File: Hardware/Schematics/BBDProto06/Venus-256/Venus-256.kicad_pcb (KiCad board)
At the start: 4 copper layers, 180.1 x 113.7 mm, 231 parts, among them J201 RaspberryPi header, J301 ARM JTAG, U1001 AD7616, U101 TPS22993, U401 AD7616, U501 ATSAME70Q21A-AN, U601 AD7616, U701 AD7616, U801 AD7616, U901 ATSAME70Q21A-AN

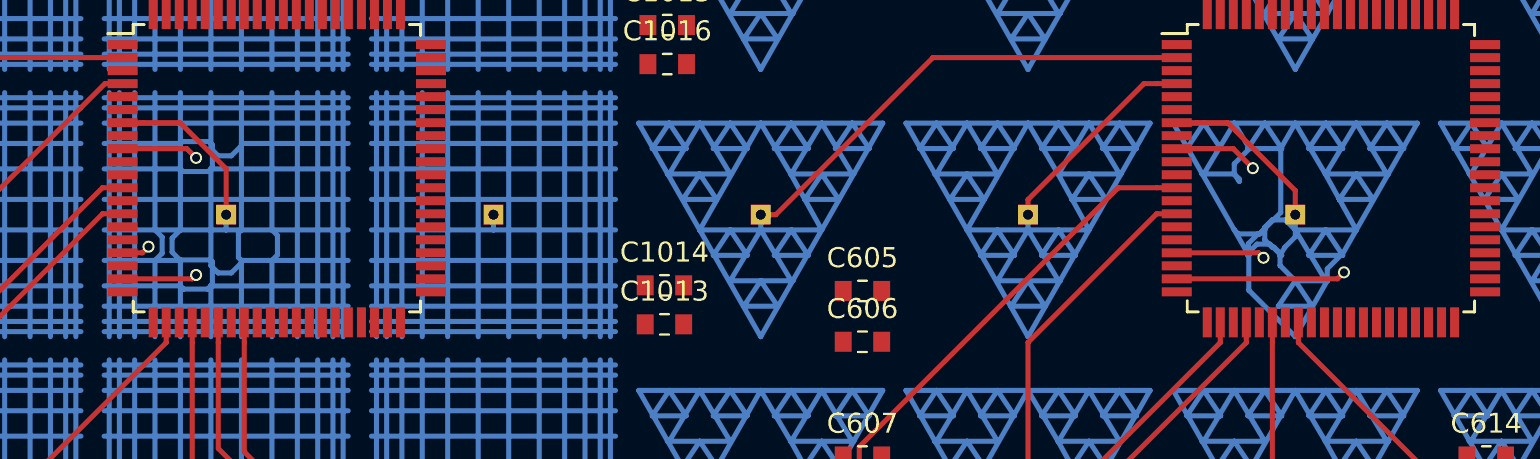
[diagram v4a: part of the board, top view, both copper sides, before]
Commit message: Fixed the antenna net mess-up
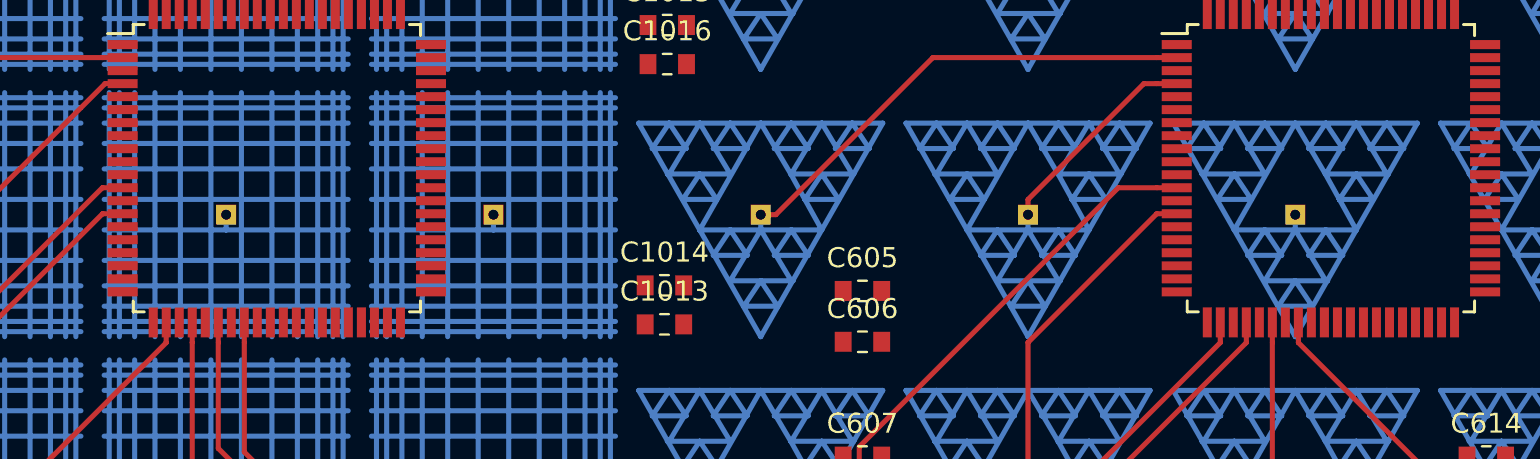
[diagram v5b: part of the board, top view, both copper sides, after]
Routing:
- net Net-(TP405-Pad1): track 219.9 -> 125.8 mm
- net Net-(TP602-Pad1): track 82.6 -> 129.6 mm
- net Net-(TP603-Pad1): track 91.7 -> 138.7 mm
- net Net-(TP609-Pad1): track 150.0 -> 125.8 mm, vias 1 -> 0
- net Net-(TP1009-Pad1): track 316.3 -> 293.4 mm, vias 1 -> 0
- net Net-(TP605-Pad1): track 146.5 -> 125.8 mm, vias 1 -> 0
- net Net-(TP1005-Pad1): track 313.3 -> 293.4 mm, vias 1 -> 0
- net Net-(TP610-Pad1): track 142.1 -> 125.8 mm, vias 1 -> 0
- net Net-(TP1010-Pad1): track 308.1 -> 293.4 mm, vias 1 -> 0
- net Net-(TP1006-Pad1): track 304.7 -> 293.4 mm
- net Net-(TP606-Pad1): track 129.5 -> 125.8 mm

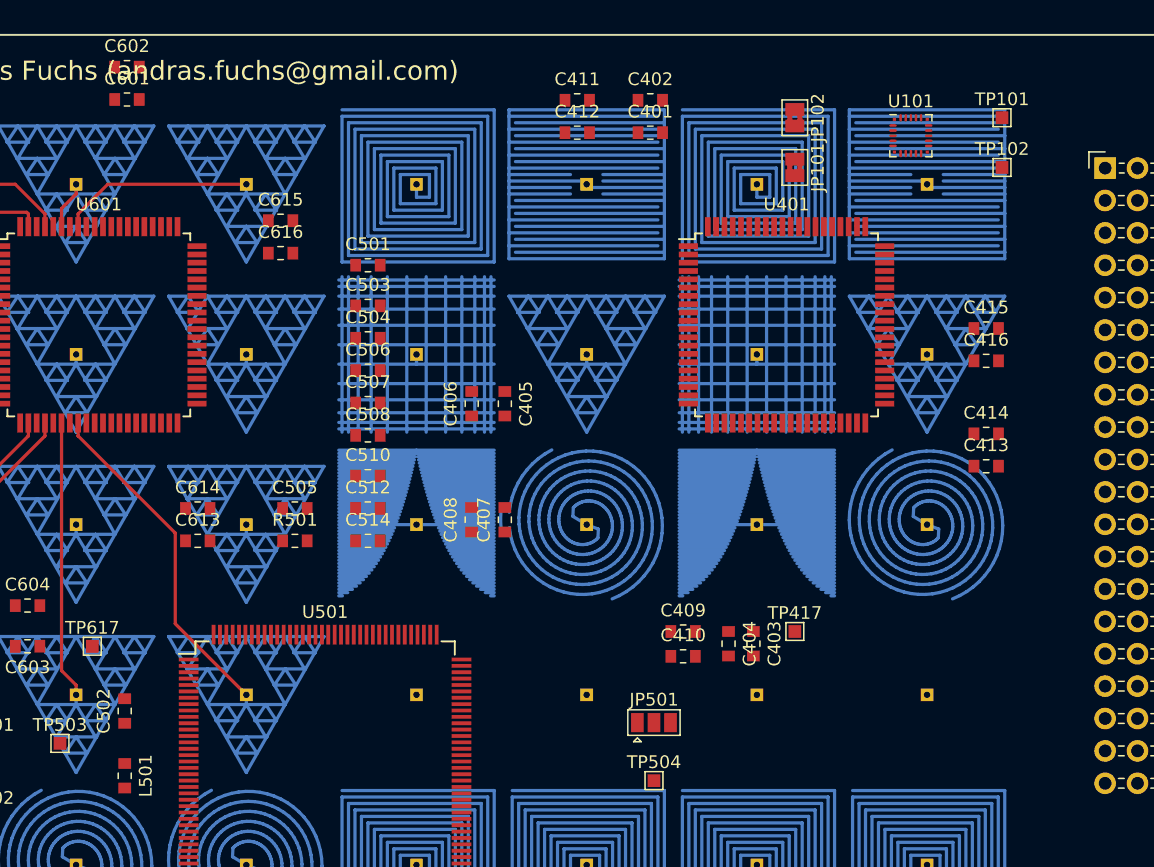
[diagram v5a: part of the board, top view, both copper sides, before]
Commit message: Removed a few tracks
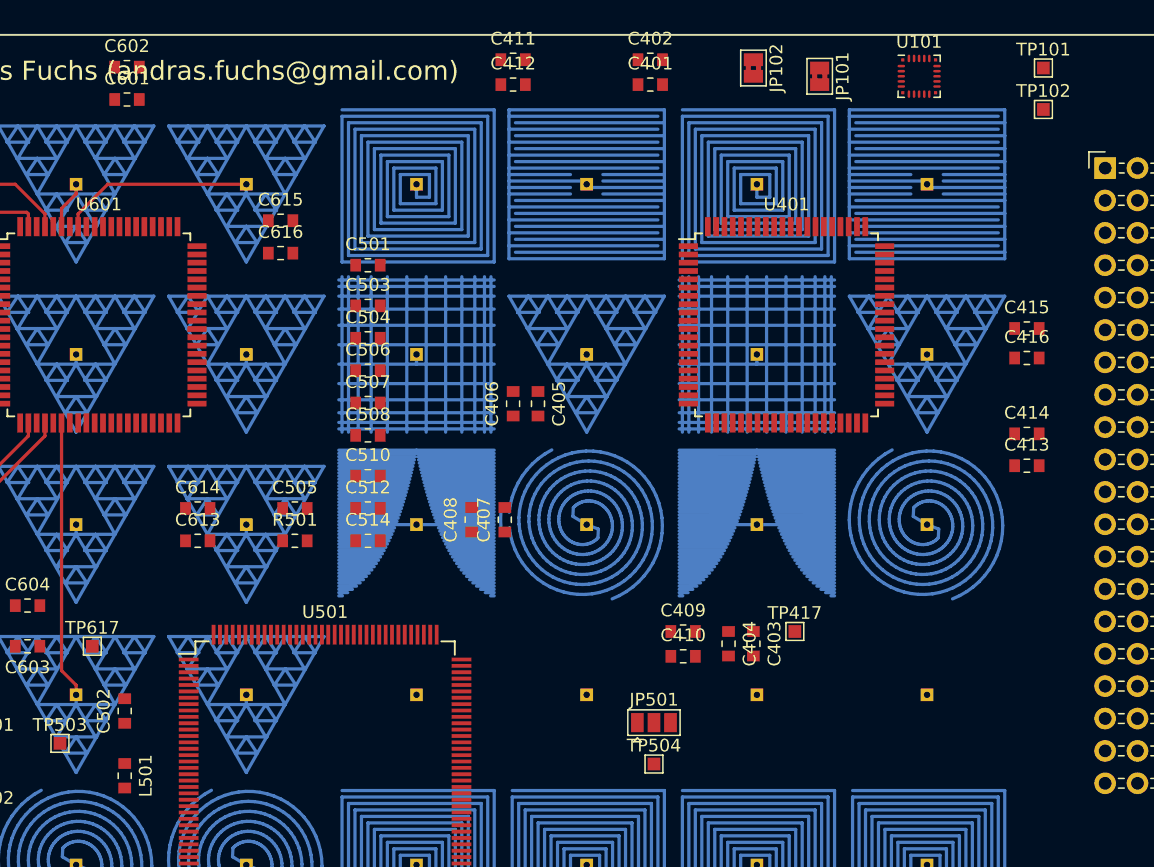
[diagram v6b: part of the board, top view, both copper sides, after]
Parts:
- moved JP101 7.41 mm to (165.1, 18.2)
- moved C412 6.29 mm to (141.1, 18.9)
- moved C411 5.95 mm to (141.1, 16.9)
- moved TP102 5.59 mm to (182.7, 20.8)
- moved JP102 5.08 mm to (159.9, 17.6)
- moved TP101 5.08 mm to (182.7, 17.6)
- moved U101 4.71 mm to (172.9, 18.2)
- moved C401 3.77 mm to (151.8, 18.9)
- moved C406 3.25 mm to (141.1, 43.9)
- moved C416 3.20 mm to (181.3, 40.3)
- moved C413 3.19 mm to (181.3, 48.8)
- moved C414 3.19 mm to (181.3, 46.2)
- moved C415 3.19 mm to (181.3, 38.0)
- moved C402 3.18 mm to (151.8, 16.9)
- moved C405 2.60 mm to (143.0, 43.9)
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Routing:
- net Net-(TP613-Pad1): track 152.6 -> 125.8 mm
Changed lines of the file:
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@@
     (thickness 1.6)
     (drawings 247)
-    (tracks 15846)
+    (tracks 15841)
     (zones 0)
     (modules 231)
@@
     (pad_to_mask_clearance 0.2)
     (aux_axis_origin 14.95 14.95)
-    (visible_elements 7FFFF7FF)
+    (visible_elements 7FFFFFFF)
     (pcbplotparams
       (layerselection 0x010fc_ffffffff)
@@
   )
   (module Capacitor_SMD:C_0603_1608Metric_Pad0.84x1.00mm_HandSolder (layer F.Cu)
-    (at 140.4 43.8875 270)
+    (at 143 43.8875 270)
     (descr "Capacitor SMD 0603 (1608 Metric), square (rectangular) end terminal, IPC_7351 nominal with elongated pad for handsoldering. (Body size source: http://www.tortai-tech.com/upload/download/2011102023233369053.pdf), generated with kicad-footprint-generator")
     (tags "capacitor handsolder")
@@
   )
   (module Capacitor_SMD:C_0603_1608Metric_Pad0.84x1.00mm_HandSolder (layer F.Cu)
-    (at 137.8 43.8875 90)
+    (at 141.05 43.8875 90)
     (descr "Capacitor SMD 0603 (1608 Metric), square (rectangular) end terminal, IPC_7351 nominal with elongated pad for handsoldering. (Body size source: http://www.tortai-tech.com/upload/download/2011102023233369053.pdf), generated with kicad-footprint-generator")
     (tags "capacitor handsolder")
@@
   )
   (module Capacitor_SMD:C_0603_1608Metric_Pad0.84x1.00mm_HandSolder (layer F.Cu)
-    (at 178.16 46.25)
+    (at 181.35 46.25)
     (descr "Capacitor SMD 0603 (1608 Metric), square (rectangular) end terminal, IPC_7351 nominal with elongated pad for handsoldering. (Body size source: http://www.tortai-tech.com/upload/download/2011102023233369053.pdf), generated with kicad-footprint-generator")
     (tags "capacitor handsolder")
@@
   )
   (module Capacitor_SMD:C_0603_1608Metric_Pad0.84x1.00mm_HandSolder (layer F.Cu)
-    (at 178.16 48.79)
+    (at 181.35 48.75)
     (descr "Capacitor SMD 0603 (1608 Metric), square (rectangular) end terminal, IPC_7351 nominal with elongated pad for handsoldering. (Body size source: http://www.tortai-tech.com/upload/download/2011102023233369053.pdf), generated with kicad-footprint-generator")
     (tags "capacitor handsolder")
@@
   )
   (module Capacitor_SMD:C_0603_1608Metric_Pad0.84x1.00mm_HandSolder (layer F.Cu)
-    (at 146.08 20.08)
+    (at 141.05 16.9)
     (descr "Capacitor SMD 0603 (1608 Metric), square (rectangular) end terminal, IPC_7351 nominal with elongated pad for handsoldering. (Body size source: http://www.tortai-tech.com/upload/download/2011102023233369053.pdf), generated with kicad-footprint-generator")
     (tags "capacitor handsolder")
@@
   )
   (module Capacitor_SMD:C_0603_1608Metric_Pad0.84x1.00mm_HandSolder (layer F.Cu)
-    (at 146.08 22.62)
+    (at 141.05 18.85)
     (descr "Capacitor SMD 0603 (1608 Metric), square (rectangular) end terminal, IPC_7351 nominal with elongated pad for handsoldering. (Body size source: http://www.tortai-tech.com/upload/download/2011102023233369053.pdf), generated with kicad-footprint-generator")
     (tags "capacitor handsolder")
@@
   )
   (module Capacitor_SMD:C_0603_1608Metric_Pad0.84x1.00mm_HandSolder (layer F.Cu)
-    (at 151.81 20.08)
+    (at 151.81 16.9)
     (descr "Capacitor SMD 0603 (1608 Metric), square (rectangular) end terminal, IPC_7351 nominal with elongated pad for handsoldering. (Body size source: http://www.tortai-tech.com/upload/download/2011102023233369053.pdf), generated with kicad-footprint-generator")
     (tags "capacitor handsolder")
@@
   )
   (module Capacitor_SMD:C_0603_1608Metric_Pad0.84x1.00mm_HandSolder (layer F.Cu)
-    (at 151.81 22.62)
+    (at 151.81 18.85)
     (descr "Capacitor SMD 0603 (1608 Metric), square (rectangular) end terminal, IPC_7351 nominal with elongated pad for handsoldering. (Body size source: http://www.tortai-tech.com/upload/download/2011102023233369053.pdf), generated with kicad-footprint-generator")
     (tags "capacitor handsolder")
@@
   )
   (module Capacitor_SMD:C_0603_1608Metric_Pad0.84x1.00mm_HandSolder (layer F.Cu)
-    (at 178.16 37.98)
+    (at 181.35 37.98)
     (descr "Capacitor SMD 0603 (1608 Metric), square (rectangular) end terminal, IPC_7351 nominal with elongated pad for handsoldering. (Body size source: http://www.tortai-tech.com/upload/download/2011102023233369053.pdf), generated with kicad-footprint-generator")
     (tags "capacitor handsolder")
@@
   )
   (module Capacitor_SMD:C_0603_1608Metric_Pad0.84x1.00mm_HandSolder (layer F.Cu)
-    (at 178.16 40.52)
+    (at 181.35 40.3)
     (descr "Capacitor SMD 0603 (1608 Metric), square (rectangular) end terminal, IPC_7351 nominal with elongated pad for handsoldering. (Body size source: http://www.tortai-tech.com/upload/download/2011102023233369053.pdf), generated with kicad-footprint-generator")
     (tags "capacitor handsolder")
@@
   )
   (module TestPoint:TestPoint_Pad_1.0x1.0mm (layer F.Cu)
-    (at 179.4 21.45)
+    (at 182.65 17.55)
     (descr "SMD rectangular pad as test Point, square 1.0mm side length")
     (tags "test point SMD pad rectangle square")
@@
   )
   (module TestPoint:TestPoint_Pad_1.0x1.0mm (layer F.Cu)
-    (at 179.4 25.35)
+    (at 182.65 20.8)
     (descr "SMD rectangular pad as test Point, square 1.0mm side length")
     (tags "test point SMD pad rectangle square")
@@
   )
   (module Package_DFN_QFN:Texas_S-PWQFN-N20 (layer F.Cu)
-    (at 172.25 22.86)
+    (at 172.9 18.2)
     (descr "20-Pin Plastic Quad Flatpack No-Lead Package, Body 3.0x3.0x0.8mm, Texas Instruments (http://www.ti.com/lit/ds/symlink/tps22993.pdf)")
     (tags "QFN 0.4")
@@
   )
   (module Jumper:SolderJumper-2_P1.3mm_Bridged2Bar_Pad1.0x1.5mm (layer F.Cu)
-    (at 163.15 25.35 270)
+    (at 165.1 18.2 270)
     (descr "SMD Solder Jumper, 1x1.5mm Pads, 0.3mm gap, bridged with 2 copper strips")
     (tags "solder jumper open")
@@
   )
   (module Jumper:SolderJumper-2_P1.3mm_Bridged2Bar_Pad1.0x1.5mm (layer F.Cu)
-    (at 163.15 21.45 270)
+    (at 159.9 17.55 270)
     (descr "SMD Solder Jumper, 1x1.5mm Pads, 0.3mm gap, bridged with 2 copper strips")
     (tags "solder jumper open")
@@
   )
   (module TestPoint:TestPoint_Pad_1.0x1.0mm (layer F.Cu)
-    (at 152.1 73.45)
+    (at 152.1 72.15)
     (descr "SMD rectangular pad as test Point, square 1.0mm side length")
     (tags "test point SMD pad rectangle square")
@@
   (segment (start 117.072 64.688) (end 115.548 64.688) (width 0.254) (layer B.Cu) (net 70))
   (segment (start 115.548 64.688) (end 115.4754 64.688) (width 0.254) (layer B.Cu) (net 70))
-  (segment (start 106.925 46.404) (end 106.925 45.4) (width 0.254) (layer F.Cu) (net 70))
-  (segment (start 106.925 46.410802) (end 106.925 46.404) (width 0.254) (layer F.Cu) (net 70))
-  (segment (start 114.543999 54.029801) (end 106.925 46.410802) (width 0.254) (layer F.Cu) (net 70))
-  (segment (start 114.543999 61.143999) (end 114.543999 54.029801) (width 0.254) (layer F.Cu) (net 70))
-  (segment (start 120.12 66.72) (end 114.543999 61.143999) (width 0.254) (layer F.Cu) (net 70))
   (segment (start 106.77 70.022) (end 105.923 71.292) (width 0.254) (layer B.Cu) (net 71))
   (segment (start 105.923 71.292) (end 107.617 71.292) (width 0.254) (layer B.Cu) (net 71))

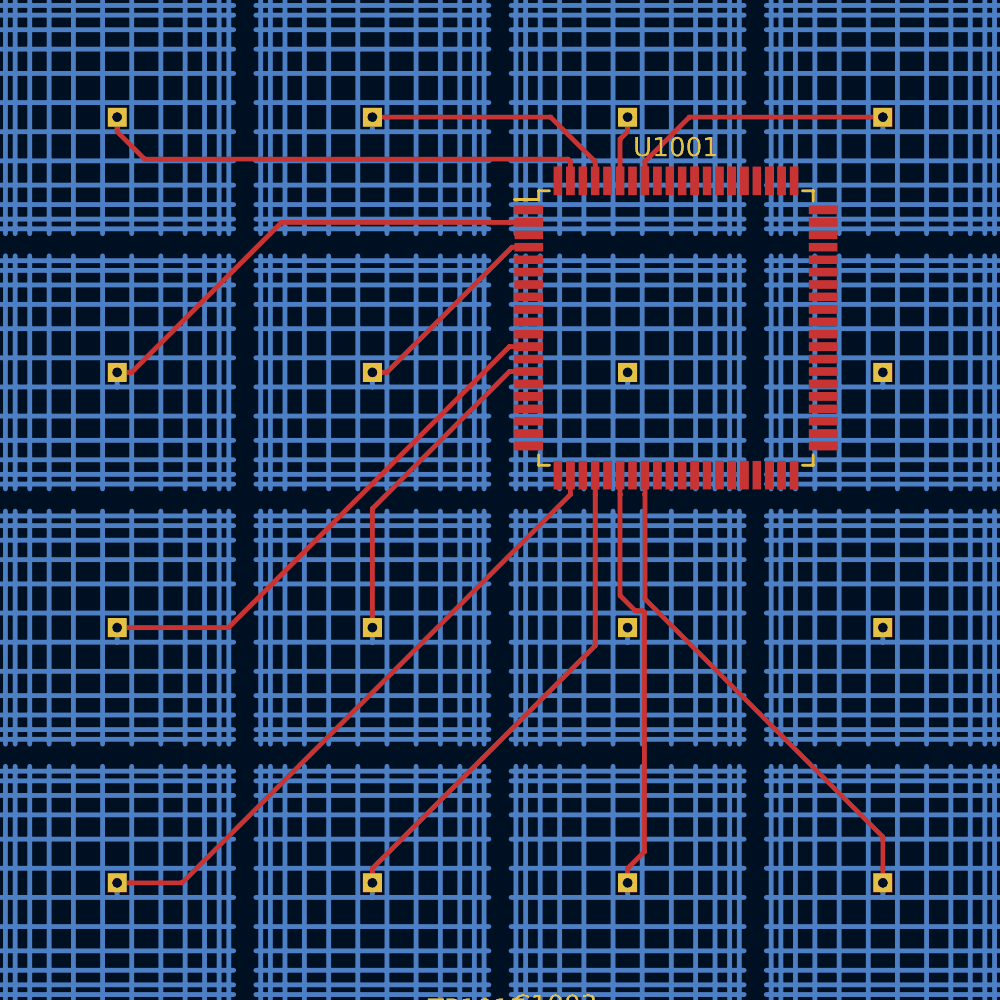
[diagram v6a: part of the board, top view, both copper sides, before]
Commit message: Connected the sensors to U1001 manually
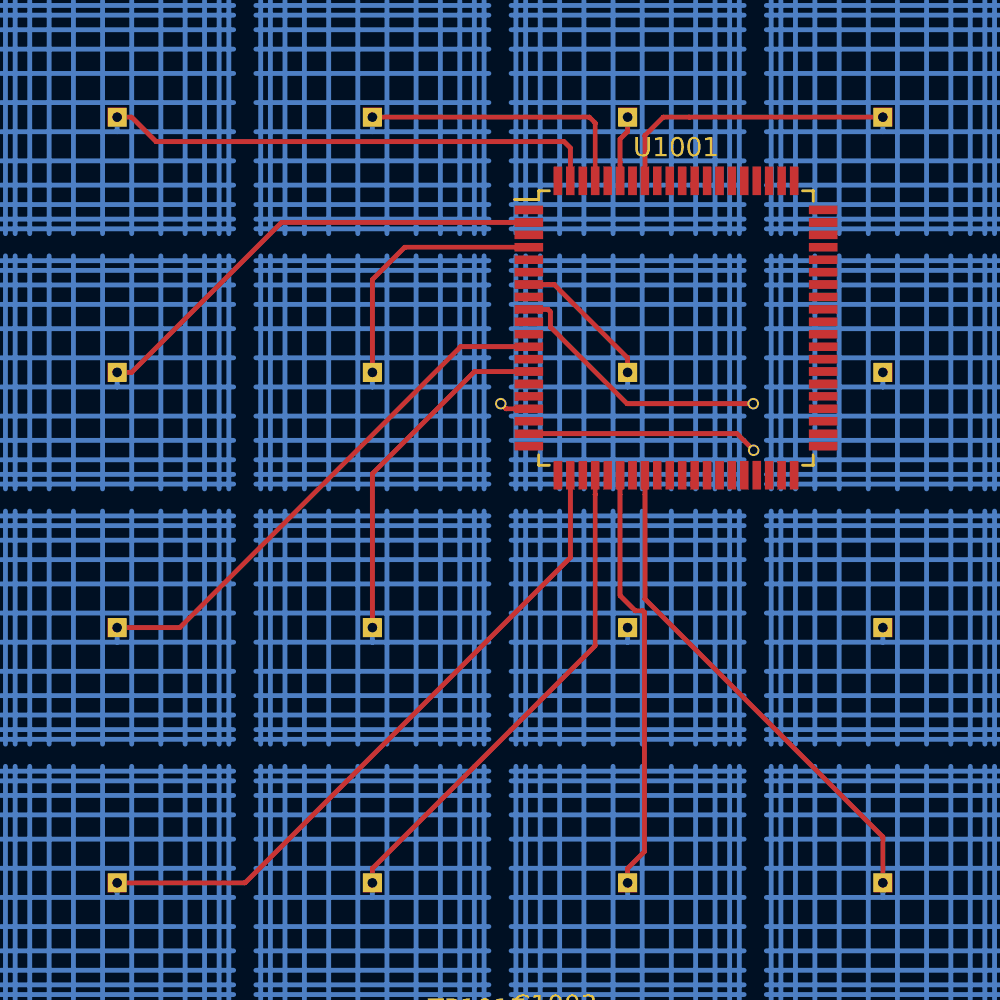
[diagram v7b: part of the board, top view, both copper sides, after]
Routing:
- net Net-(TP1009-Pad1): track 293.4 -> 317.6 mm, vias 0 -> 1
- net Net-(TP1005-Pad1): track 293.4 -> 315.1 mm, vias 0 -> 1
- net Net-(TP1010-Pad1): track 293.4 -> 315.0 mm, vias 0 -> 1
- net Net-(TP1006-Pad1): track 293.4 -> 300.9 mm
- net Net-(TP1007-Pad1): track 304.3 -> 307.1 mm
- net Net-(TP1016-Pad1): track 326.5 -> 328.4 mm
- net Net-(TP1003-Pad1): track 307.0 -> 308.2 mm
- net Net-(TP1011-Pad1): track 310.7 -> 311.8 mm
- net Net-(TP1001-Pad1): track 307.8 -> 308.6 mm
